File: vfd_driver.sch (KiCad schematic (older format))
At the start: 48 parts, among them J2 futaba_7_lt_44z, J3 Input, Q1 IRLZ34, Q2 IRF640, Q3 BC817, Q4 BC807, Q5 BC817, Q6 BC807, T1 Transformer_1P_SS, U2 74HC595, U3 74HC595, U4 74HC595, U5 TBD62783A, U6 TBD62783A, U7 TBD62783A

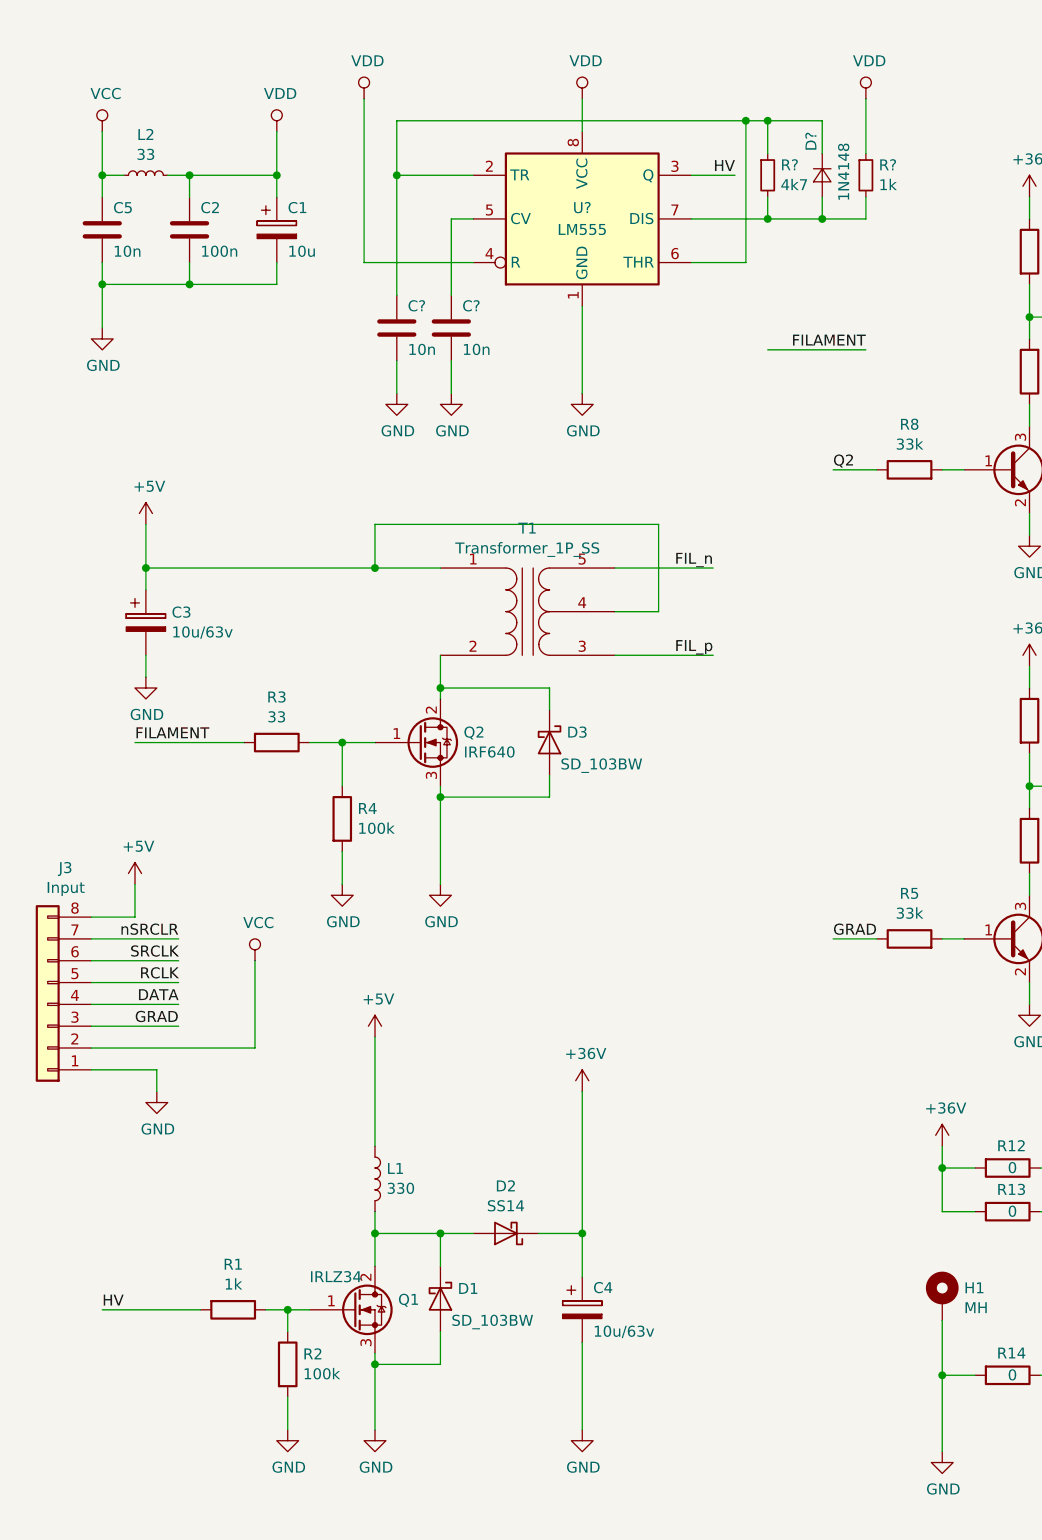
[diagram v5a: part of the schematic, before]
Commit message: Add lm4871
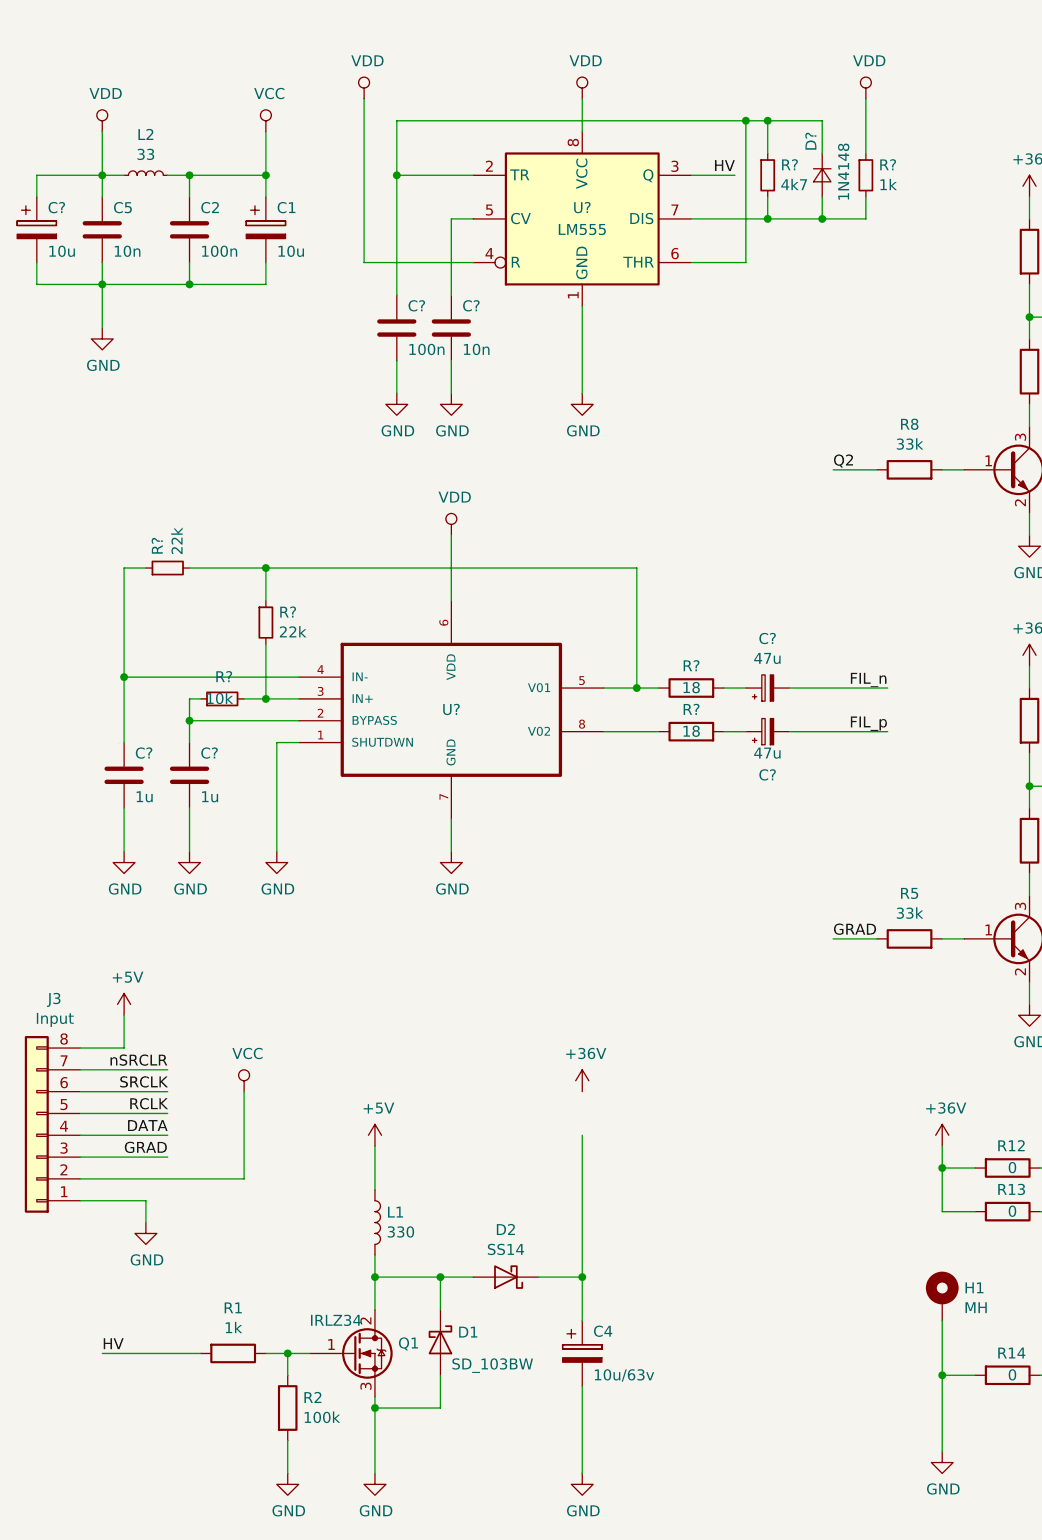
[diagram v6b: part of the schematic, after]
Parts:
- removed C3: 10u/63v, Capacitor_THT:CP_Radial_D8.0mm_P5.00mm, symbol Device:CP
- removed D3: SD_103BW, Diode_SMD:D_SOD-123, symbol Device:D_Schottky
- removed Q2: IRF640, Package_TO_SOT_THT:TO-220-3_Vertical, symbol Device:Q_NMOS_GDS
- removed R3: 33, Resistor_SMD:R_0805_2012Metric_Pad1.15x1.40mm_HandSolder, symbol Device:R
- removed R4: 100k, Resistor_SMD:R_0805_2012Metric_Pad1.15x1.40mm_HandSolder, symbol Device:R
- removed T1: Transformer_1P_SS, custom_footprint:Transformer_toroid_v_18mm, symbol Device:Transformer_1P_SS
- added C? (x2): 1u, Capacitor_SMD:C_0805_2012Metric_Pad1.15x1.40mm_HandSolder, symbol Device:C
- added C?: 10u, Capacitor_THT:CP_Radial_D8.0mm_P3.80mm, symbol Device:CP
- added C? (x2): 47u, symbol Device:CP_Small
- added R?: 10k, Resistor_SMD:R_0805_2012Metric_Pad1.15x1.40mm_HandSolder, symbol Device:R_Small
- added R? (x2): 22k, Resistor_SMD:R_0805_2012Metric_Pad1.15x1.40mm_HandSolder, symbol Device:R_Small
- added R? (x2): 18, Resistor_SMD:R_0805_2012Metric_Pad1.15x1.40mm_HandSolder, symbol Device:R
- added U?: LM4871, SO08, symbol LM4871:LM4871
- C?: value 10n -> 100n
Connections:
- net +36V: no longer C4.1, D2.1 (K)
- net FIL_n: now also C?.2
- net FIL_p: now also C?.2
- net GND: now also C?.2, C?.2, C?.2, U?.1 (SHUTDWN), U?.7 (GND)
- net VCC: now also C1.1, C2.1, L2.2; no longer C5.1, L2.1
- net VDD: now also C5.1, L2.1, C?.1, U?.6 (VDD); no longer C1.1, C2.1, L2.2
- new net: C4.1, D2.1 (K)
- new net: C?.1, R?.1, U?.2 (BYPASS)
- new net: R?.2, R?.2, U?.3 (IN+)
- new net: C?.1, R?.1, U?.4 (IN-)
- new net: R?.1, R?.1, R?.2, U?.5 (V01)
- new net: R?.1, U?.8 (V02)
- new net: C?.1, R?.2 (x2)
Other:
- moved on the sheet: C1, C4, D1, D2, J3, L1, Q1, R1, R2

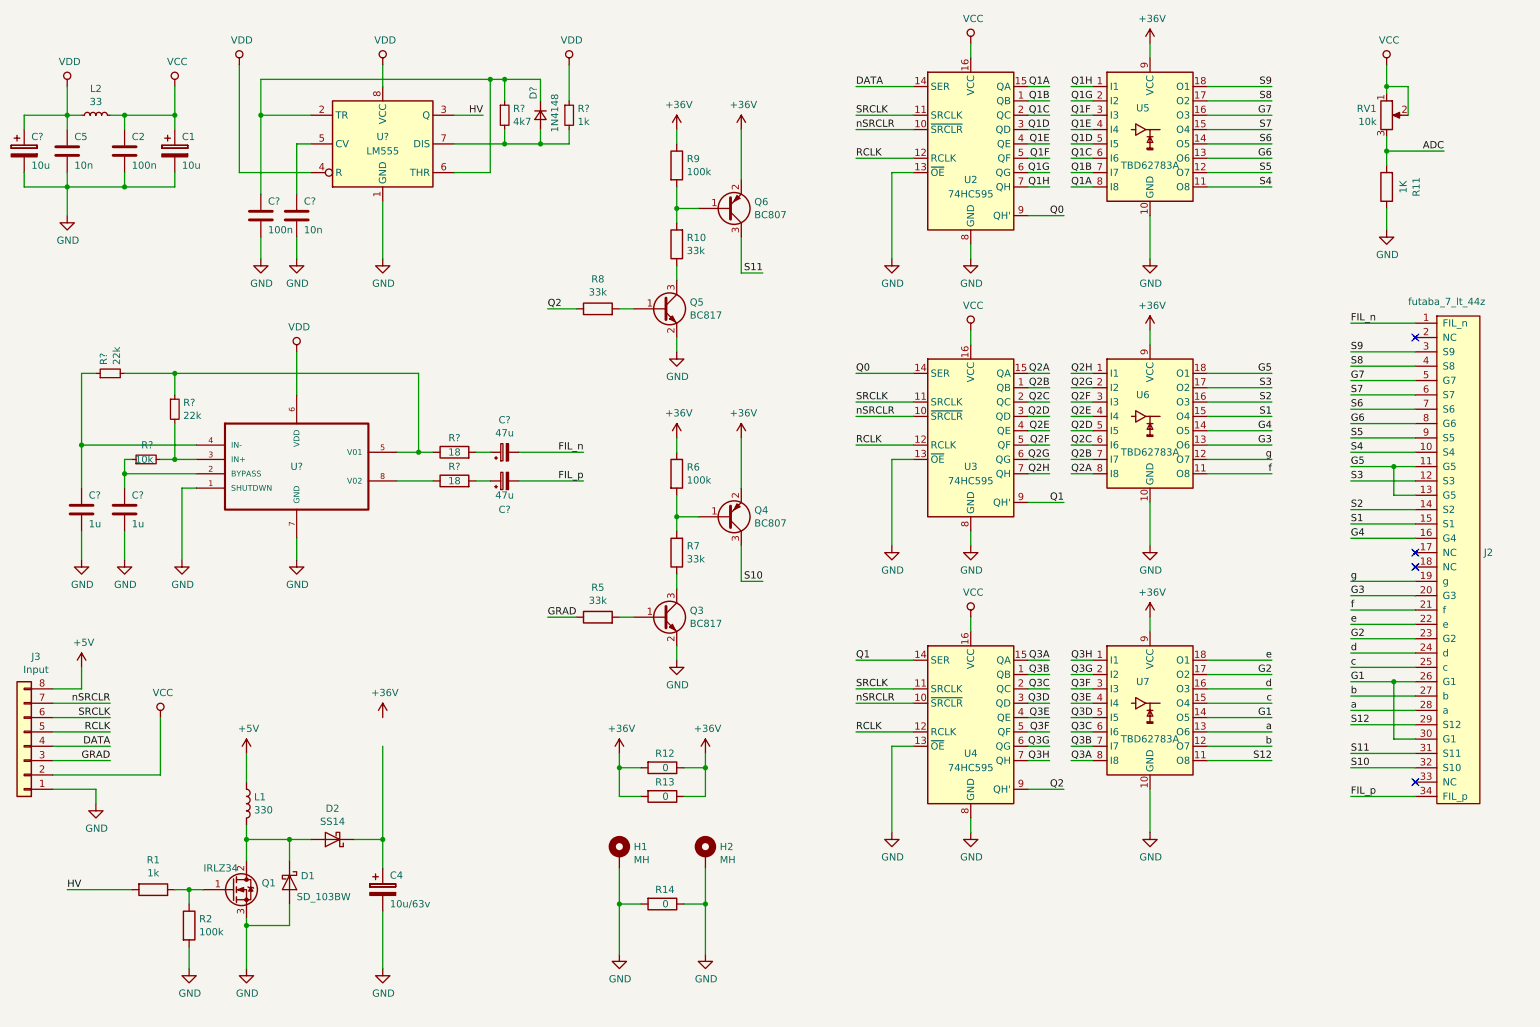
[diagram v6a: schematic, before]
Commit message: pwr and logic separed
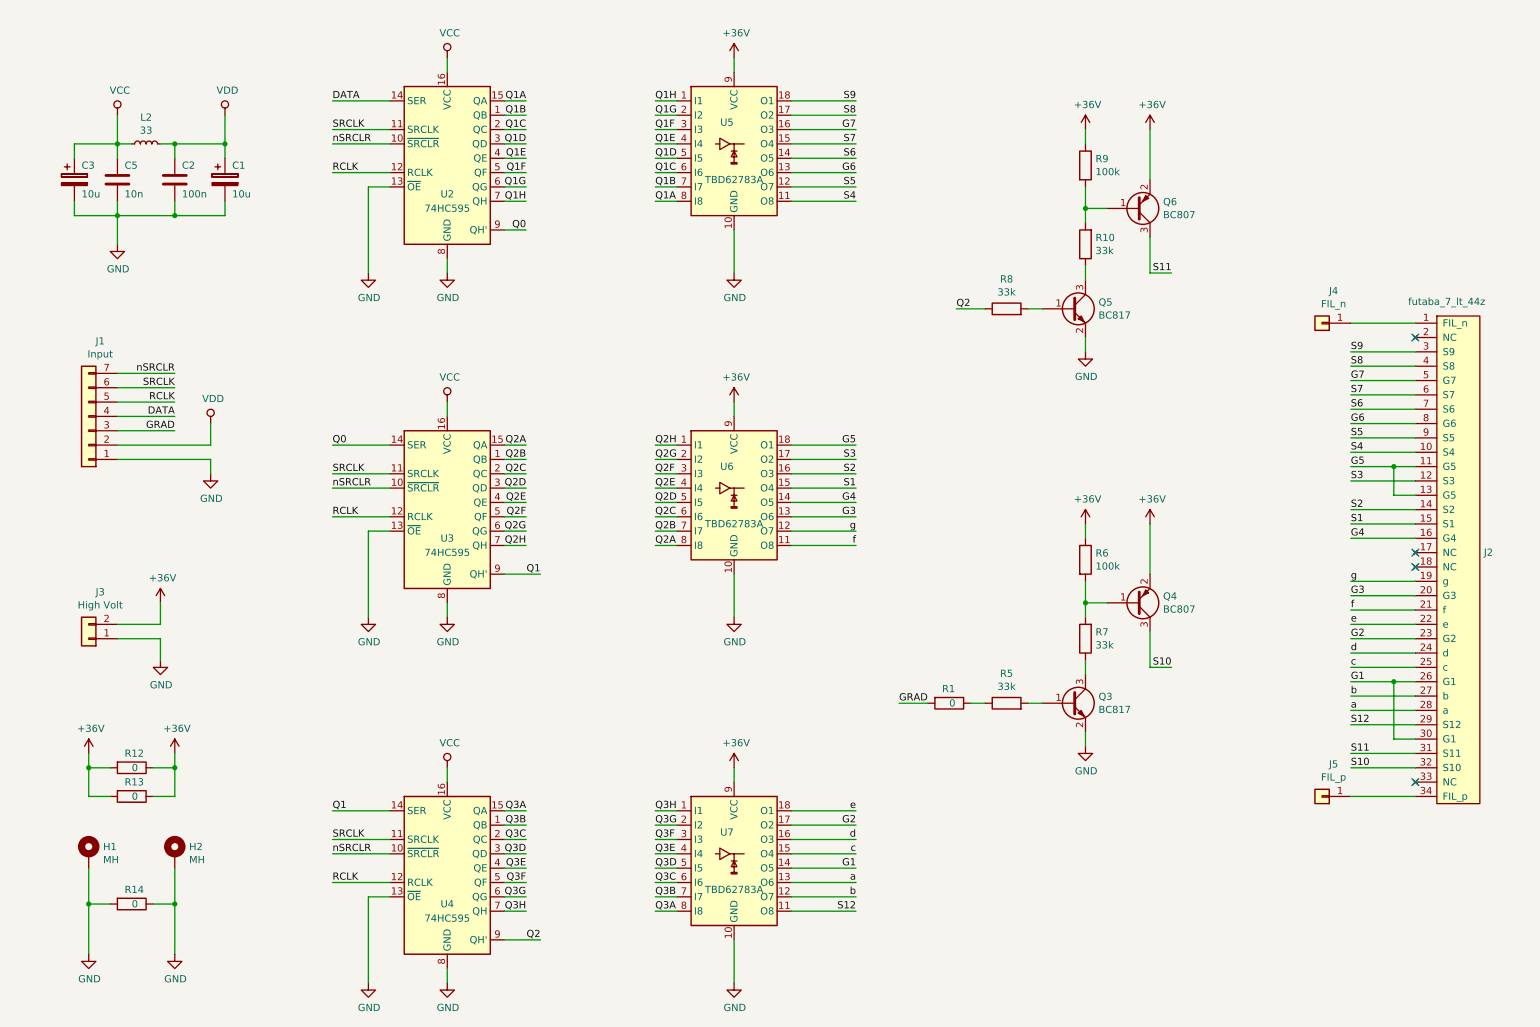
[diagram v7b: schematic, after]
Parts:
- removed C4: 10u/63v, Capacitor_THT:CP_Radial_D8.0mm_P5.00mm, symbol Device:CP
- removed C?: 10n, Capacitor_SMD:C_0805_2012Metric_Pad1.15x1.40mm_HandSolder, symbol Device:C
- removed C?: 100n, Capacitor_SMD:C_0805_2012Metric_Pad1.15x1.40mm_HandSolder, symbol Device:C
- removed C? (x2): 1u, Capacitor_SMD:C_0805_2012Metric_Pad1.15x1.40mm_HandSolder, symbol Device:C
- removed C? (x2): 47u, symbol Device:CP_Small
- removed D1: SD_103BW, Diode_SMD:D_SOD-123, symbol Device:D_Schottky
- removed D2: SS14, Diode_SMD:D_SMA_Handsoldering, symbol Device:D_Schottky
- removed D?: 1N4148, symbol Device:D_Small
- removed J3: Input, Connector_PinHeader_2.54mm:PinHeader_1x08_P2.54mm_Vertical, symbol Connector_Generic:Conn_01x08
- removed L1: 330, Choke_SMD:Choke_CD75, symbol Device:L
- removed Q1: IRLZ34, Package_TO_SOT_THT:TO-220-3_Vertical, symbol Device:Q_NMOS_GDS
- removed R11: 1K, Resistor_SMD:R_0805_2012Metric_Pad1.15x1.40mm_HandSolder, symbol Device:R
- removed R2: 100k, Resistor_SMD:R_0805_2012Metric_Pad1.15x1.40mm_HandSolder, symbol Device:R
- removed R?: 1k, Resistor_SMD:R_0805_2012Metric_Pad1.15x1.40mm_HandSolder, symbol Device:R_Small
- removed R?: 4k7, Resistor_SMD:R_0805_2012Metric_Pad1.15x1.40mm_HandSolder, symbol Device:R_Small
- removed R?: 10k, Resistor_SMD:R_0805_2012Metric_Pad1.15x1.40mm_HandSolder, symbol Device:R_Small
- removed R? (x2): 22k, Resistor_SMD:R_0805_2012Metric_Pad1.15x1.40mm_HandSolder, symbol Device:R_Small
- removed R? (x2): 18, Resistor_SMD:R_0805_2012Metric_Pad1.15x1.40mm_HandSolder, symbol Device:R
- removed RV1: 10k, Connector_PinHeader_2.54mm:PinHeader_1x03_P2.54mm_Vertical, symbol Device:R_POT
- removed U?: LM555, symbol Timer:LM555
- removed U?: LM4871, SO08, symbol LM4871:LM4871
- added J1: Input, Connector_PinSocket_2.54mm:PinSocket_1x07_P2.54mm_Vertical, symbol Connector_Generic:Conn_01x07
- added J3: High Volt, Connector_PinHeader_2.54mm:PinHeader_1x02_P2.54mm_Vertical, symbol Connector_Generic:Conn_01x02
- added J4: FIL_n, Connector_Pin:Pin_D1.4mm_L8.5mm_W2.8mm_FlatFork, symbol Connector_Generic:Conn_01x01
- added J5: FIL_p, Connector_Pin:Pin_D1.4mm_L8.5mm_W2.8mm_FlatFork, symbol Connector_Generic:Conn_01x01
- R1: value 1k -> 0; footprint Resistor_SMD:R_0805_2012Metric_Pad1.15x1.40mm_HandSolder -> Resistor_SMD:R_1206_3216Metric
- gave numbers to parts that had none: 1
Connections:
- net HV is gone; now on net GRAD: R1.2
- net +36V: now also J3.2 (Pin_2)
- net DATA: now also J1.4 (Pin_4)
- net GND: now also J1.1 (Pin_1), J3.1 (Pin_1)
- net GRAD: now also J1.3 (Pin_3); no longer R5.1
- net RCLK: now also J1.5 (Pin_5)
- net SRCLK: now also J1.6 (Pin_6)
- net VCC: now also C3.1, C5.1, L2.1; no longer C1.1, C2.1, L2.2
- net VDD: now also C1.1, C2.1, L2.2, J1.2 (Pin_2); no longer C3.1, C5.1, L2.1
- net nSRCLR: now also J1.7 (Pin_7)
- net at R1.1: now also R5.1
- net FIL_n: no longer names the net of J2.1 (FIL_n)
- net FIL_n: now also J4.1 (Pin_1)
- net FIL_p: no longer names the net of J2.34 (FIL_p)
- net FIL_p: now also J5.1 (Pin_1)
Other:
- moved on the sheet: C1, C2, C3, C5, H1, H2, L2, Q3, Q4, Q5, Q6, R10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
